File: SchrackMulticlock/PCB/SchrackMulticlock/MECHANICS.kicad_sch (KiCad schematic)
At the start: 34 parts, among them SW2 SW_Push, SW3 SW_Push, SW4 SW_Push, SW5 SW_Push, SW6 SW_Push, SW7 SW_Push, SW8 SW_Push, SW9 SW_Push, U8 74HC14

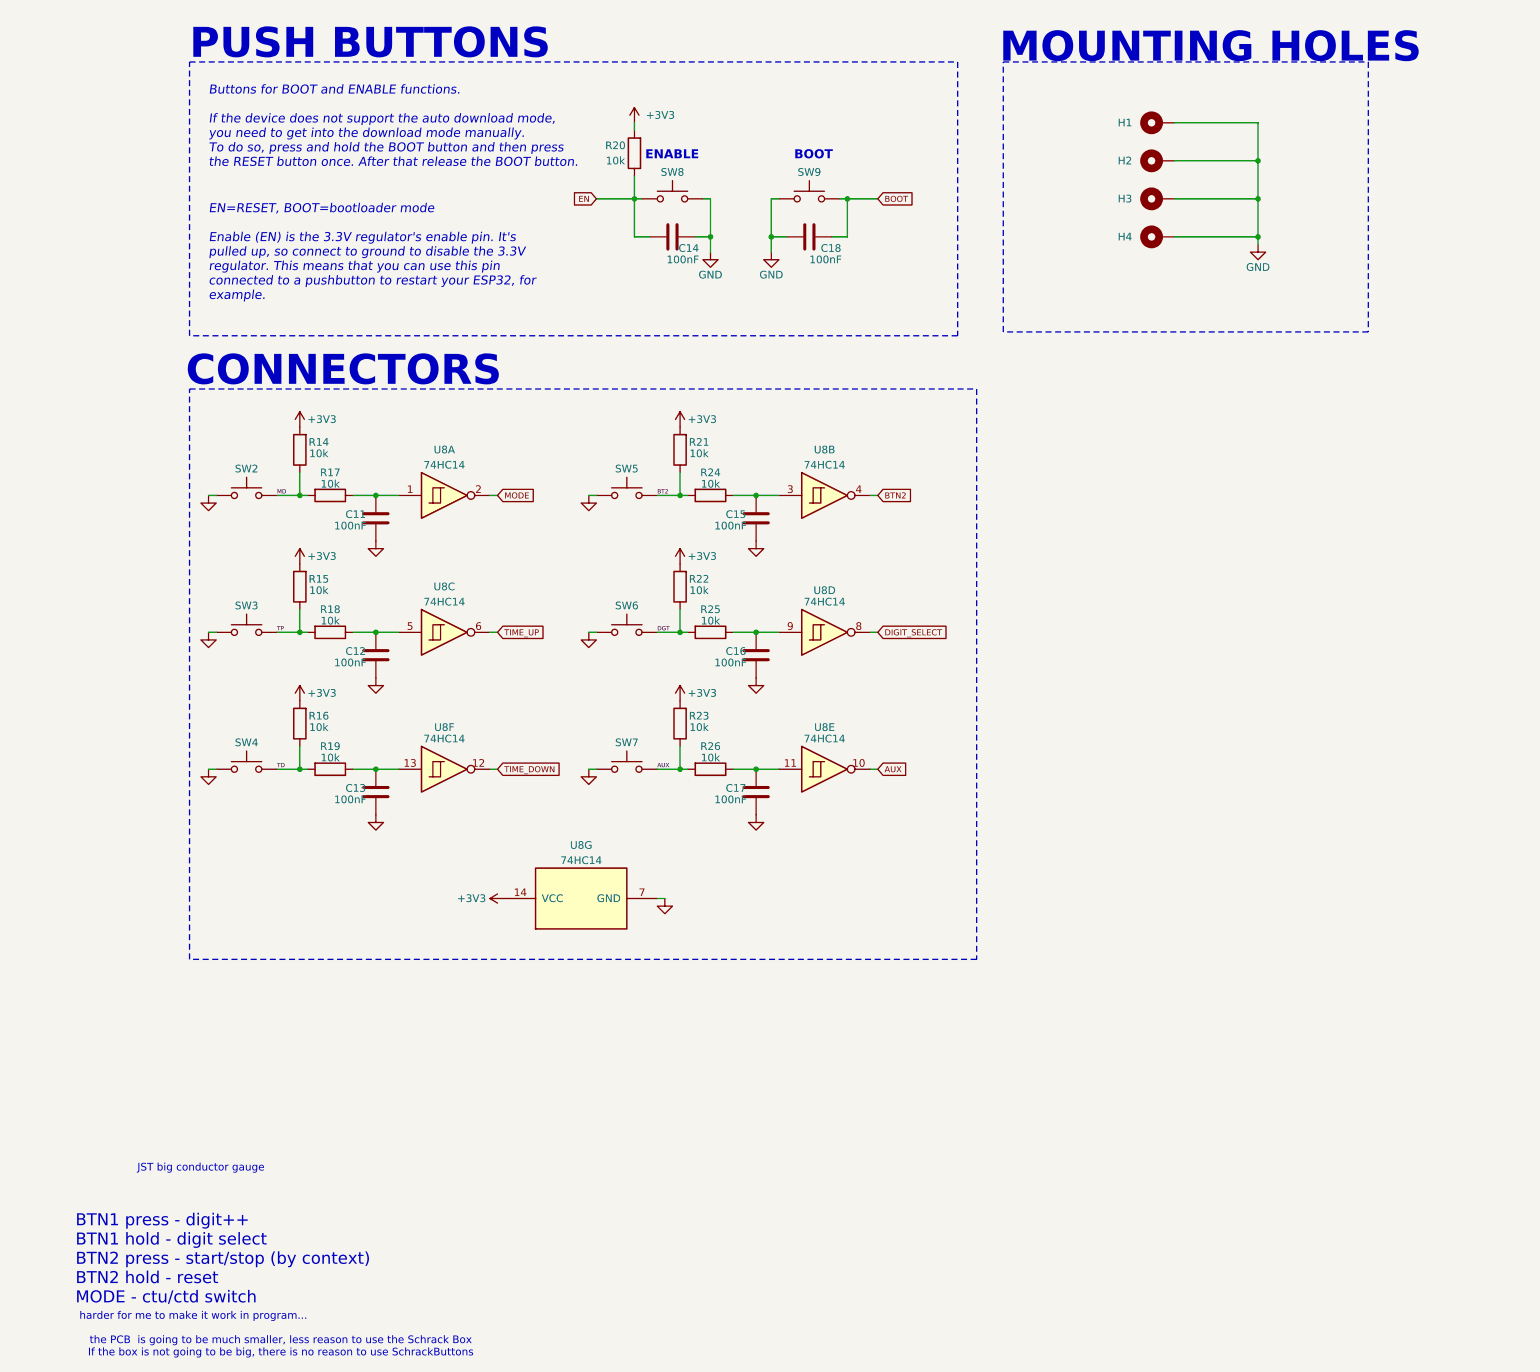
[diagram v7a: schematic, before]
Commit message: SchrackMulticlock PCB final routing
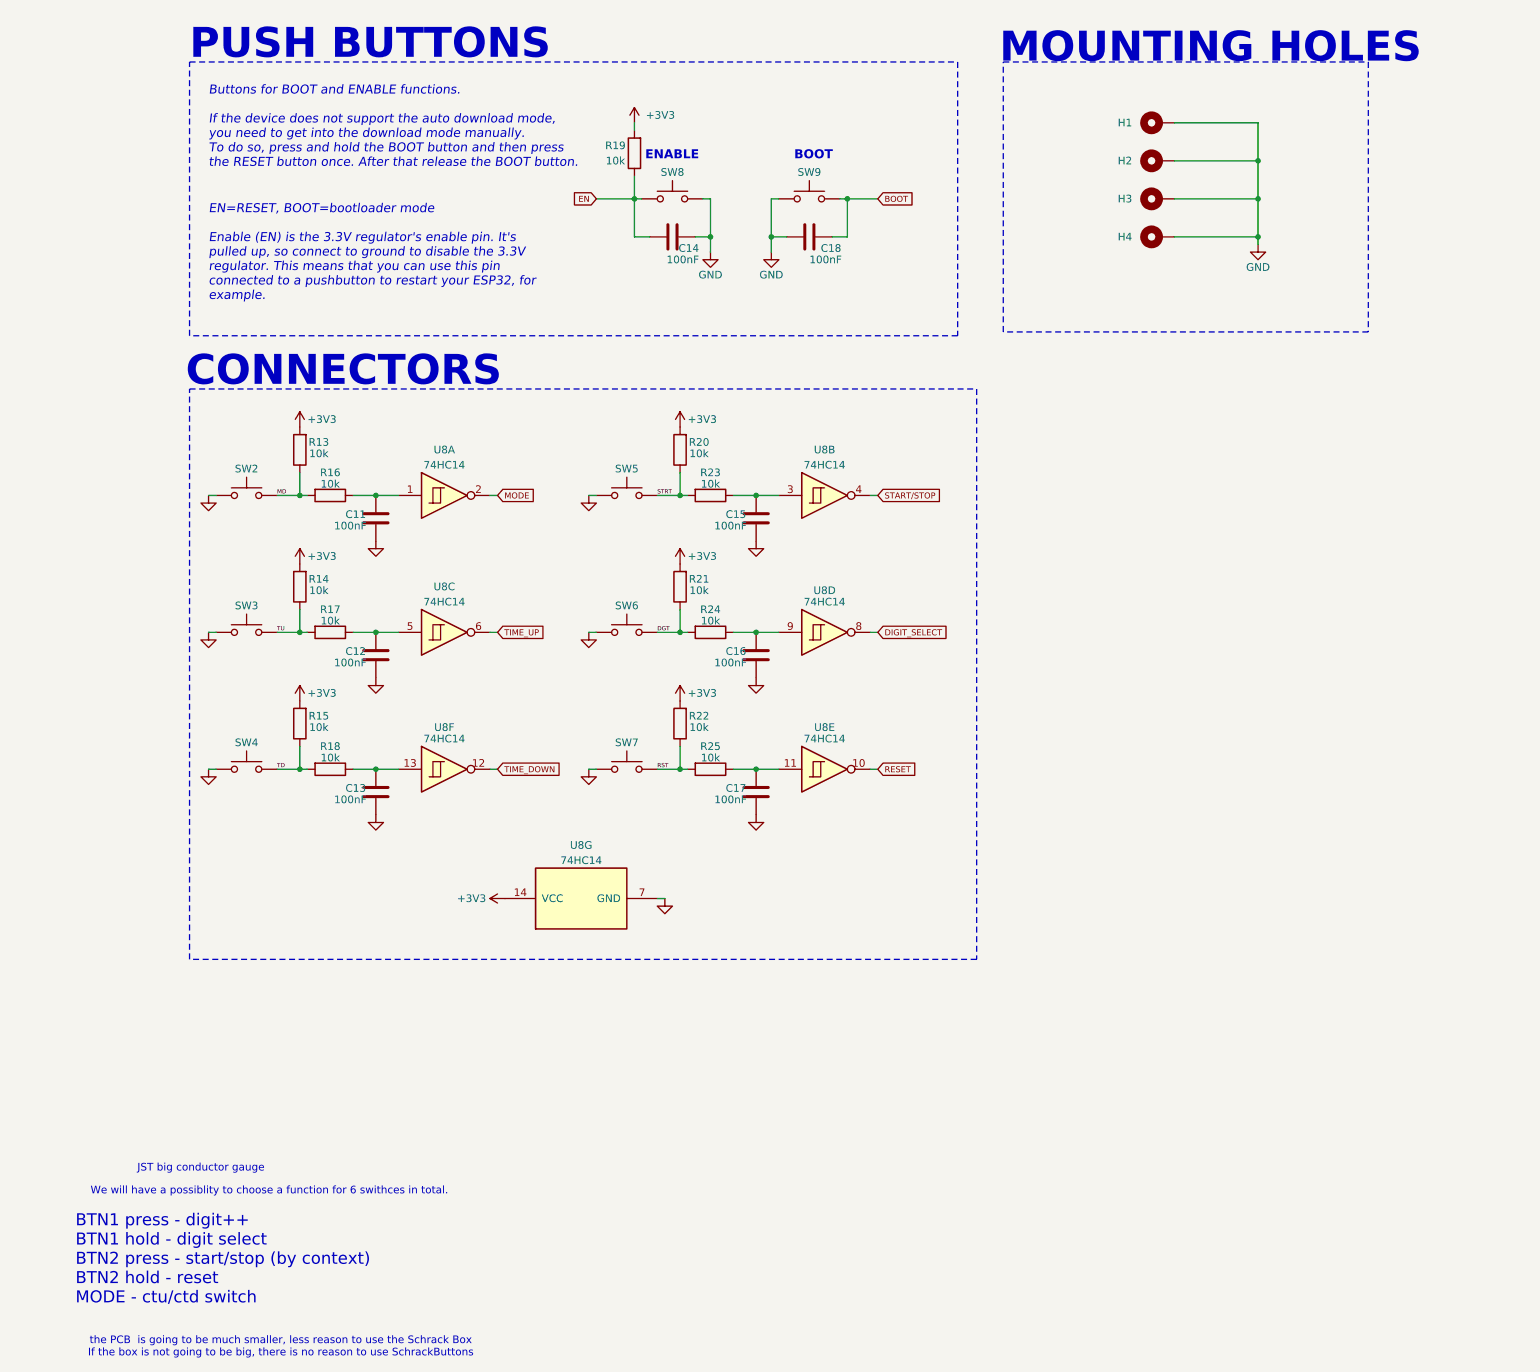
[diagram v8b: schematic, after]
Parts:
- renumbered R14 to R13, R15 to R14, R16 to R15, R17 to R16, R18 to R17, R19 to R18, R20 to R19, R21 to R20, R22 to R21, R23 to R22, R24 to R23, R25 to R24, R26 to R25
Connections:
- net AUX renamed RST
- net RST: no longer U8.10
- net BT2 renamed STRT
- net BTN2 renamed START/STOP
- net TP renamed TU
- new net RESET: U8.10
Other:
- note added: "We will have a possiblity to choose a function for 6 swithces in total."
- note removed: "harder for me to make it work in program..."
